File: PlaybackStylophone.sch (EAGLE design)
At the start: 51 parts, among them SW6 ON/OFF

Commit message: Updated AUTODESK files
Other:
- moved on the sheet: LEFT_HEADER, RIGHT_HEADER

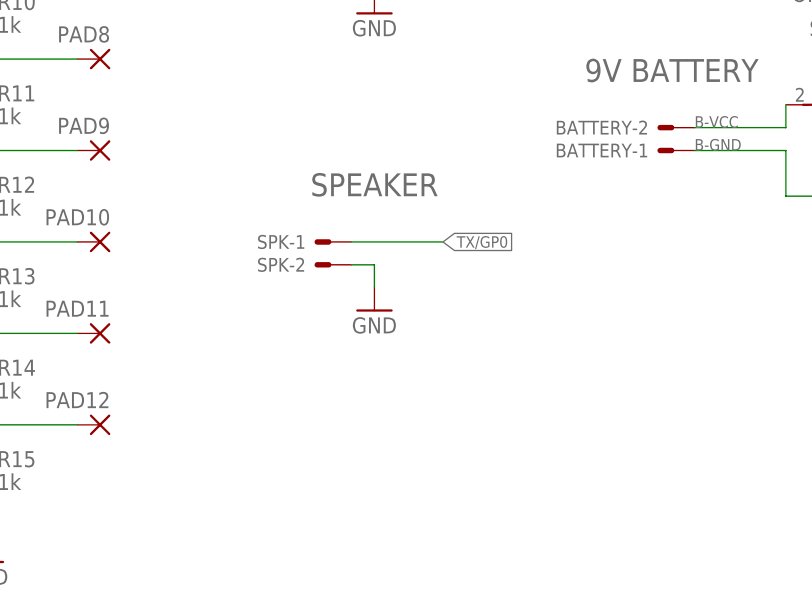
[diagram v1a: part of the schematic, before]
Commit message: Added low-pass filter
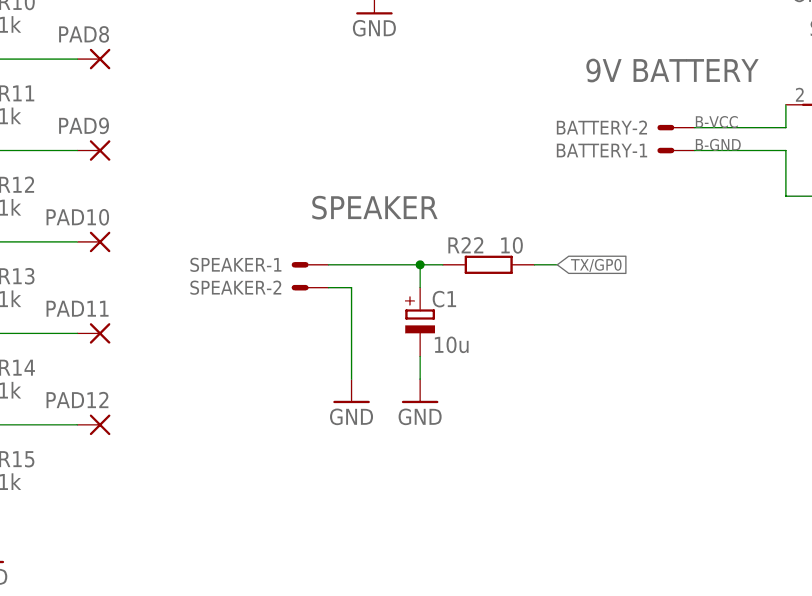
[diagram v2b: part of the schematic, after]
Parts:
- removed SPK: SPEAKER, con-molex:22-23-2021
- added C1: 10u, rcl:CPOL-EUE2.5-5
- added R22: 10, rcl:R-EU_0204/7
- added SPEAKER: SPEAKER, con-molex:22-23-2021
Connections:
- new net N$1: C1.+, R22.2, SPEAKER-1.S
- net GND: now also C1.-, SPEAKER-2.S; no longer SPK-2.S
- net TX/GP0: now also R22.1; no longer SPK-1.S
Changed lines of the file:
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@@
 <setting verticaltext="up"/>
 </settings>
-<grid distance="0.1" unitdist="inch" unit="inch" style="lines" multiple="1" display="no" altdistance="0.01" altunitdist="inch" altunit="inch"/>
+<grid distance="0.1" unitdist="inch" unit="inch" style="lines" multiple="1" display="yes" altdistance="0.01" altunitdist="inch" altunit="inch"/>
 <layers>
 <layer number="1" name="Top" color="4" fill="1" visible="no" active="no"/>
@@
 <part name="PAD12" library="wirepad" library_urn="urn:adsk.eagle:library:412" deviceset="SMD5" device="" package3d_urn="urn:adsk.eagle:package:30841/1"/>
 <part name="GND3" library="supply1" library_urn="urn:adsk.eagle:library:371" deviceset="GND" device=""/>
-<part name="SPK" library="con-molex" library_urn="urn:adsk.eagle:library:165" deviceset="22-23-2021" device="" package3d_urn="urn:adsk.eagle:package:8078633/1" value="SPEAKER"/>
+<part name="SPEAKER" library="con-molex" library_urn="urn:adsk.eagle:library:165" deviceset="22-23-2021" device="" package3d_urn="urn:adsk.eagle:package:8078633/1" value="SPEAKER"/>
 <part name="DISPLAY" library="pinhead" library_urn="urn:adsk.eagle:library:325" deviceset="PINHD-1X4" device="" package3d_urn="urn:adsk.eagle:package:22407/2" value="GND"/>
 <part name="GND5" library="supply1" library_urn="urn:adsk.eagle:library:371" deviceset="GND" device=""/>
@@
 <part name="GND1" library="supply1" library_urn="urn:adsk.eagle:library:371" deviceset="GND" device=""/>
 <part name="R2" library="rcl" library_urn="urn:adsk.eagle:library:334" deviceset="R-EU_" device="0204/7" package3d_urn="urn:adsk.eagle:package:23498/2" value="10k"/>
+<part name="R22" library="rcl" library_urn="urn:adsk.eagle:library:334" deviceset="R-EU_" device="0204/7" package3d_urn="urn:adsk.eagle:package:23498/2" value="10"/>
+<part name="C1" library="rcl" library_urn="urn:adsk.eagle:library:334" deviceset="CPOL-EU" device="E2.5-5" package3d_urn="urn:adsk.eagle:package:23344/1" value="10u"/>
+<part name="GND4" library="supply1" library_urn="urn:adsk.eagle:library:371" deviceset="GND" device=""/>
 </parts>
 <sheets>
@@
 <attribute name="VALUE" x="20.32" y="10.16" size="1.778" layer="96" align="bottom-center"/>
 </instance>
-<instance part="SPK" gate="-1" x="58.42" y="48.26" smashed="yes" rot="MR0">
-<attribute name="NAME" x="55.88" y="47.498" size="1.524" layer="95" rot="MR0"/>
-<attribute name="VALUE" x="63.5" y="53.34" size="2.54" layer="96" rot="MR0" align="bottom-center"/>
-</instance>
-<instance part="SPK" gate="-2" x="58.42" y="45.72" smashed="yes" rot="MR0">
-<attribute name="NAME" x="55.88" y="44.958" size="1.524" layer="95" rot="MR0"/>
+<instance part="SPEAKER" gate="-1" x="55.88" y="45.72" smashed="yes" rot="MR0">
+<attribute name="NAME" x="53.34" y="44.958" size="1.524" layer="95" rot="MR0"/>
+<attribute name="VALUE" x="63.5" y="50.8" size="2.54" layer="96" rot="MR0" align="bottom-center"/>
+</instance>
+<instance part="SPEAKER" gate="-2" x="55.88" y="43.18" smashed="yes" rot="MR0">
+<attribute name="NAME" x="53.34" y="42.418" size="1.524" layer="95" rot="MR0"/>
 </instance>
 <instance part="DISPLAY" gate="A" x="53.34" y="86.36" smashed="yes" rot="R180">
@@
 <attribute name="VALUE" x="233.68" y="143.51" size="1.778" layer="96" align="bottom-center"/>
 </instance>
-<instance part="GND1" gate="1" x="63.5" y="40.64" smashed="yes">
-<attribute name="VALUE" x="63.5" y="38.1" size="1.778" layer="96" align="bottom-center"/>
+<instance part="GND1" gate="1" x="60.96" y="30.48" smashed="yes">
+<attribute name="VALUE" x="60.96" y="27.94" size="1.778" layer="96" align="bottom-center"/>
 </instance>
 <instance part="R2" gate="G$1" x="63.5" y="134.62" smashed="yes" rot="R90">
 <attribute name="NAME" x="64.77" y="135.89" size="1.778" layer="95" align="center-left"/>
 <attribute name="VALUE" x="64.77" y="133.35" size="1.778" layer="96" align="center-left"/>
+</instance>
+<instance part="R22" gate="G$1" x="76.2" y="45.72" smashed="yes" rot="R180">
+<attribute name="NAME" x="73.66" y="46.99" size="1.778" layer="95" align="bottom-center"/>
+<attribute name="VALUE" x="78.74" y="46.99" size="1.778" layer="96" align="bottom-center"/>
+</instance>
+<instance part="C1" gate="G$1" x="68.58" y="40.64" smashed="yes">
+<attribute name="NAME" x="69.85" y="41.91" size="1.778" layer="95" align="center-left"/>
+<attribute name="VALUE" x="69.977" y="36.83" size="1.778" layer="96" align="center-left"/>
+</instance>
+<instance part="GND4" gate="1" x="68.58" y="30.48" smashed="yes">
+<attribute name="VALUE" x="68.58" y="27.94" size="1.778" layer="96" align="bottom-center"/>
 </instance>
 </instances>
@@
 </segment>
 <segment>
-<pinref part="SPK" gate="-2" pin="S"/>
-<wire x1="60.96" y1="45.72" x2="63.5" y2="45.72" width="0.1524" layer="91"/>
-<wire x1="63.5" y1="45.72" x2="63.5" y2="43.18" width="0.1524" layer="91"/>
+<pinref part="SPEAKER" gate="-2" pin="S"/>
+<wire x1="58.42" y1="43.18" x2="60.96" y2="43.18" width="0.1524" layer="91"/>
+<wire x1="60.96" y1="43.18" x2="60.96" y2="33.02" width="0.1524" layer="91"/>
 <pinref part="GND1" gate="1" pin="GND"/>
+</segment>
+<segment>
+<pinref part="C1" gate="G$1" pin="-"/>
+<pinref part="GND4" gate="1" pin="GND"/>
+<wire x1="68.58" y1="35.56" x2="68.58" y2="33.02" width="0.1524" layer="91"/>
 </segment>
 </net>
@@
 </segment>
 <segment>
-<pinref part="SPK" gate="-1" pin="S"/>
-<wire x1="60.96" y1="48.26" x2="71.12" y2="48.26" width="0.1524" layer="91"/>
-<label x="71.12" y="48.26" size="1.27" layer="95" xref="yes"/>
+<label x="83.82" y="45.72" size="1.27" layer="95" xref="yes"/>
+<pinref part="R22" gate="G$1" pin="1"/>
+<wire x1="83.82" y1="45.72" x2="81.28" y2="45.72" width="0.1524" layer="91"/>
 </segment>
 </net>
@@
 </segment>
 </net>
+<net name="N$1" class="0">
+<segment>
+<pinref part="C1" gate="G$1" pin="+"/>
+<pinref part="R22" gate="G$1" pin="2"/>
+<wire x1="68.58" y1="43.18" x2="68.58" y2="45.72" width="0.1524" layer="91"/>
+<wire x1="68.58" y1="45.72" x2="71.12" y2="45.72" width="0.1524" layer="91"/>
+<pinref part="SPEAKER" gate="-1" pin="S"/>
+<wire x1="68.58" y1="45.72" x2="58.42" y2="45.72" width="0.1524" layer="91"/>
+<junction x="68.58" y="45.72"/>
+</segment>
+</net>
